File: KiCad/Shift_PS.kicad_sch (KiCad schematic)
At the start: 37 parts

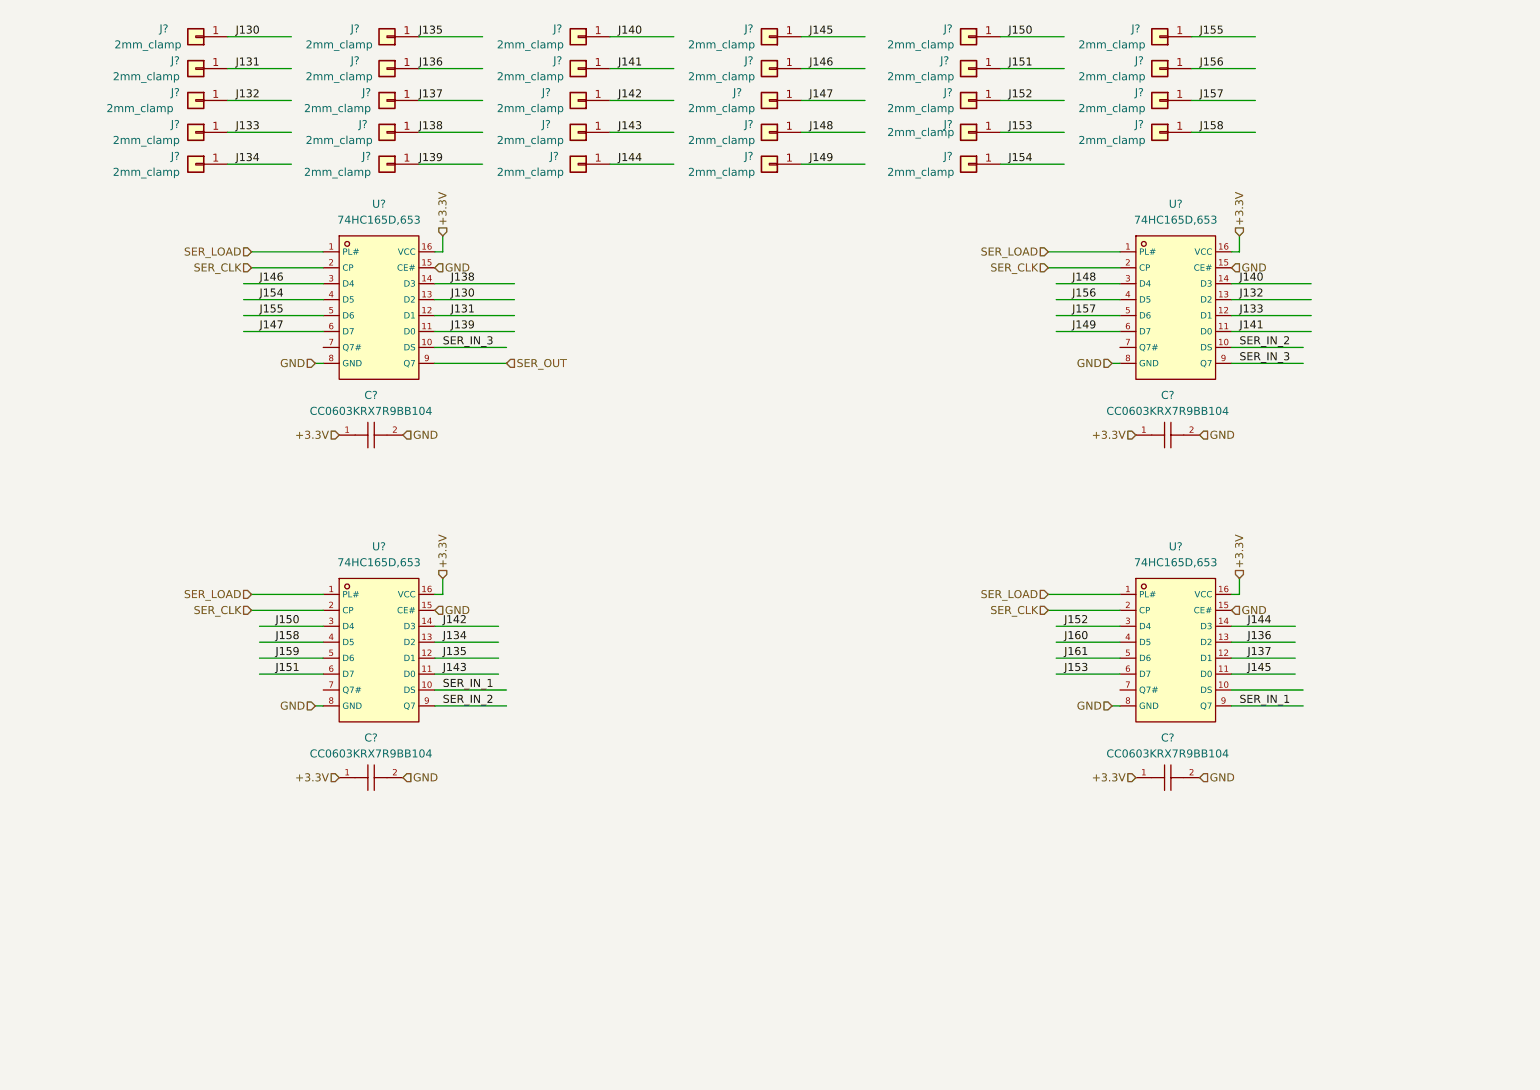
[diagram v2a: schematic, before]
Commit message: UPdated outline + added pull down resistors on input of shifts
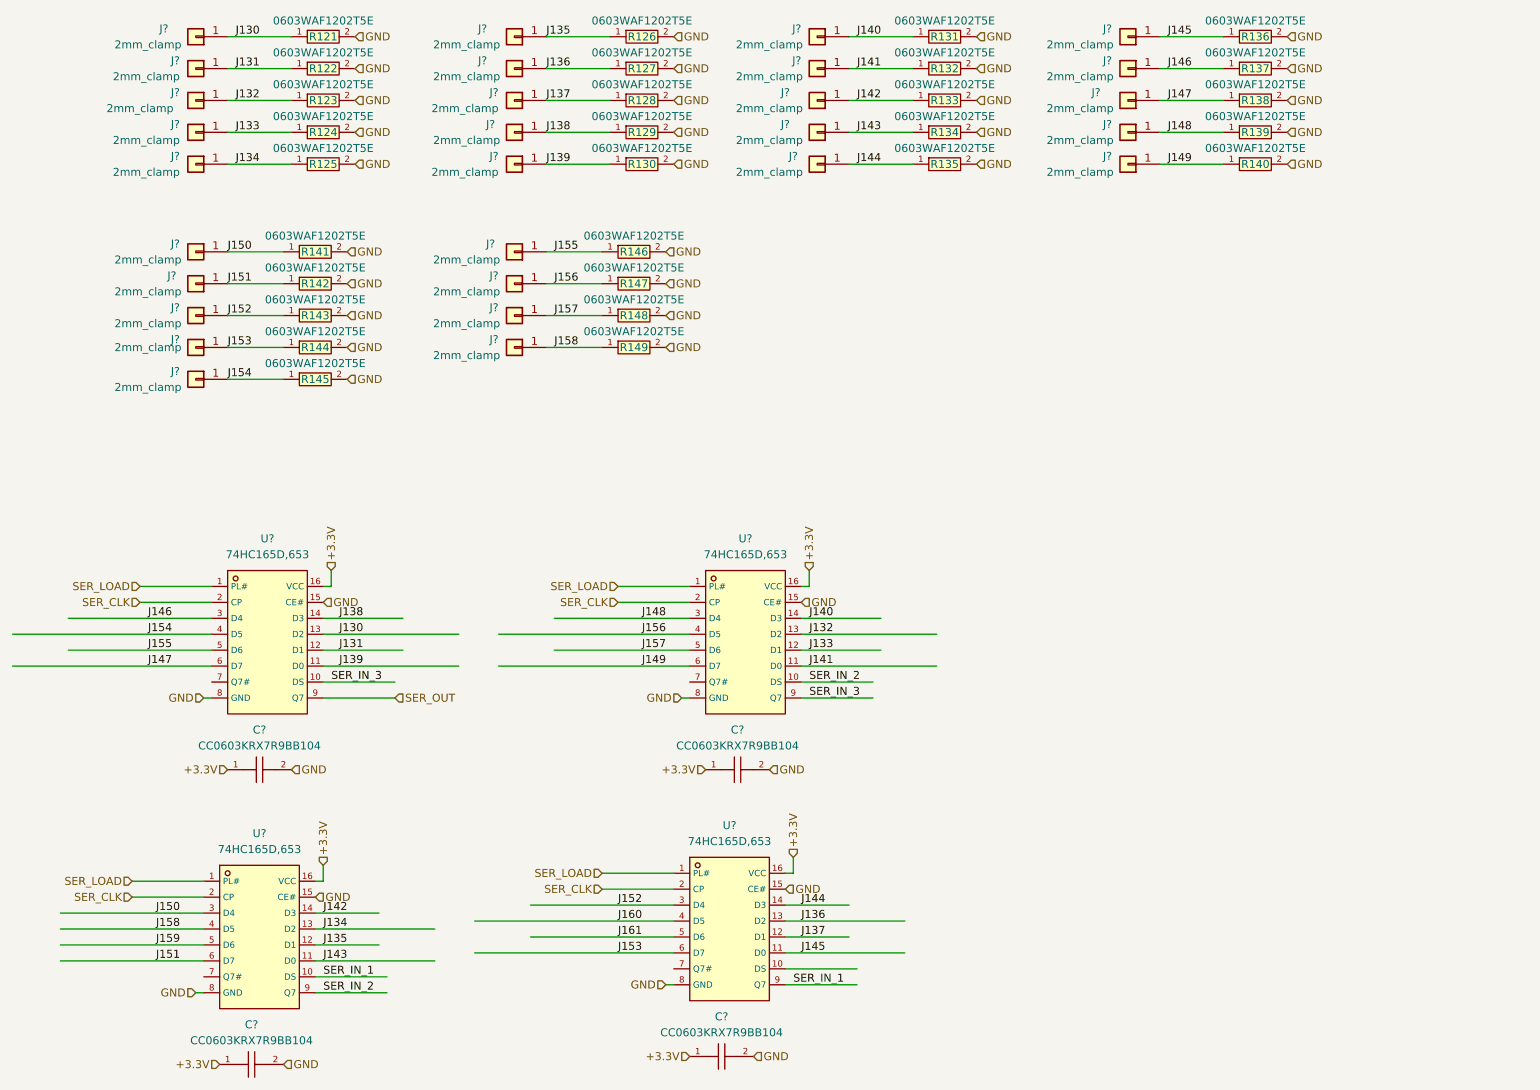
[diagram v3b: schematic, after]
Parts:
- added R121, R122, R123, R124, R125, R126, R127, R128, R129, R130, R131, R132, R133, R134, R135, R136, R137, R138, R139, R140, R141, R142, R143, R144, R145, R146, R147, R148, R149: 0603WAF1202T5E, footprint:R0603, symbol 0603WAF1202T5E:0603WAF1202T5E
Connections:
- net GND: now also R121.2, R122.2, R123.2, R124.2, R125.2, R126.2, R127.2, R128.2, R129.2, R130.2, R131.2, R132.2, R133.2, R134.2, R135.2, R136.2, R137.2, R138.2, R139.2, R140.2, R141.2, R142.2, R143.2, R144.2, R145.2, R146.2, R147.2, R148.2, R149.2
- net J130: now also R121.1
- net J131: now also R122.1
- net J132: now also R123.1
- net J133: now also R124.1
- net J134: now also R125.1
- net J135: now also R126.1
- net J136: now also R127.1
- net J137: now also R128.1
- net J138: now also R129.1
- net J139: now also R130.1
- net J140: now also R131.1
- net J141: now also R132.1
- net J142: now also R133.1
- net J143: now also R134.1
- net J144: now also R135.1
- net J145: now also R136.1
- net J146: now also R137.1
- net J147: now also R138.1
- net J148: now also R139.1
- net J149: now also R140.1
- net J150: now also R141.1
- net J151: now also R142.1
- net J152: now also R143.1
- net J153: now also R144.1
- net J154: now also R145.1
- net J155: now also R146.1
- net J156: now also R147.1
- net J157: now also R148.1
- net J158: now also R149.1
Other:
- moved on the sheet: C?, J?, U?

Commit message: First production
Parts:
- gave numbers to parts that had none: 37

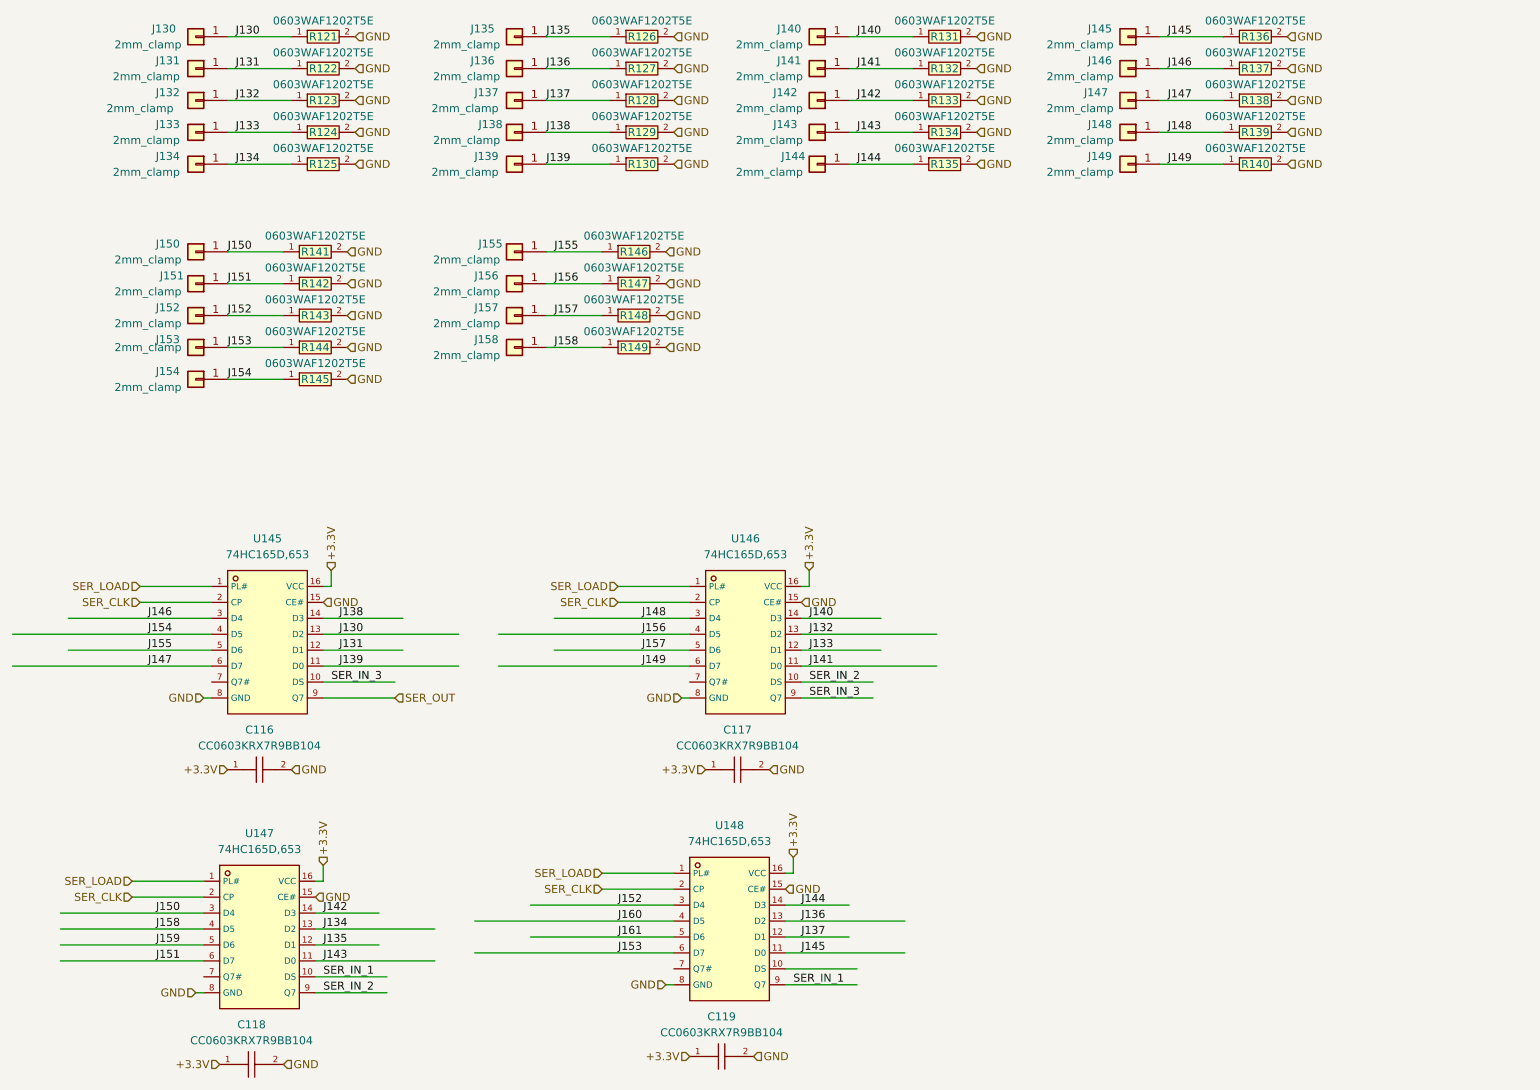
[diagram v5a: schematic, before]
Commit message: Ready for PCB layout with discreet LEDs
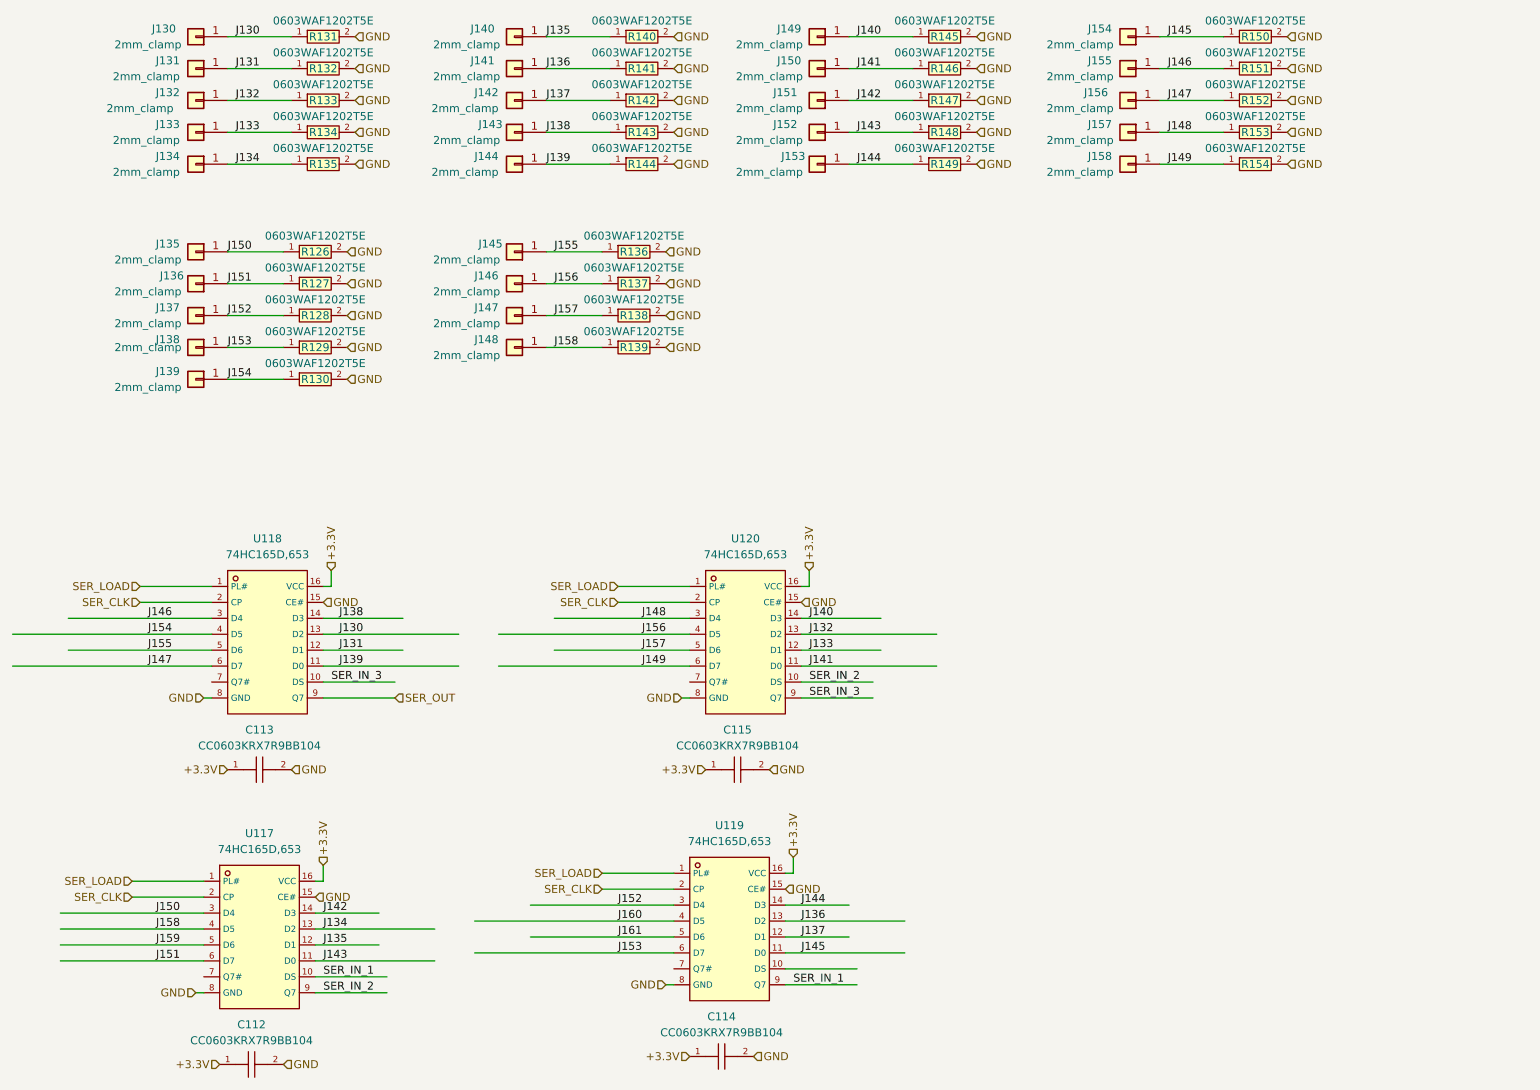
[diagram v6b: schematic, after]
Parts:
- renumbered C118 to C112, C116 to C113, C119 to C114, C117 to C115, J150 to J135, J151 to J136, J152 to J137, J153 to J138, J154 to J139, J135 to J140, J136 to J141, J137 to J142, J138 to J143, J139 to J144, J155 to J145, J156 to J146, J157 to J147, J158 to J148, J140 to J149, J141 to J150, J142 to J151, J143 to J152, J144 to J153, J145 to J154, J146 to J155, J147 to J156, J148 to J157, J149 to J158, R141 to R126, R142 to R127, R143 to R128, R144 to R129, R145 to R130, R121 to R131, R122 to R132, R123 to R133, R124 to R134, R125 to R135, R146 to R136, R147 to R137, R148 to R138, R149 to R139, R126 to R140, R127 to R141, R128 to R142, R129 to R143, R130 to R144, R131 to R145, R132 to R146, R133 to R147, R134 to R148, R135 to R149, R136 to R150, R137 to R151, R138 to R152, R139 to R153, R140 to R154, U147 to U117, U145 to U118, U148 to U119, U146 to U120
